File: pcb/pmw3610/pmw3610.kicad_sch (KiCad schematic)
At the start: 21 parts, among them J1 Conn_01x01_Socket, J2 Conn_01x01_Socket, J3 Conn_01x01_Socket, J5 Conn_01x01_Socket, J6 Conn_01x01_Socket, J7 Conn_01x01_Socket, J8 Conn_01x01_Socket, U1 TCR2EF19, U2 PMW3610

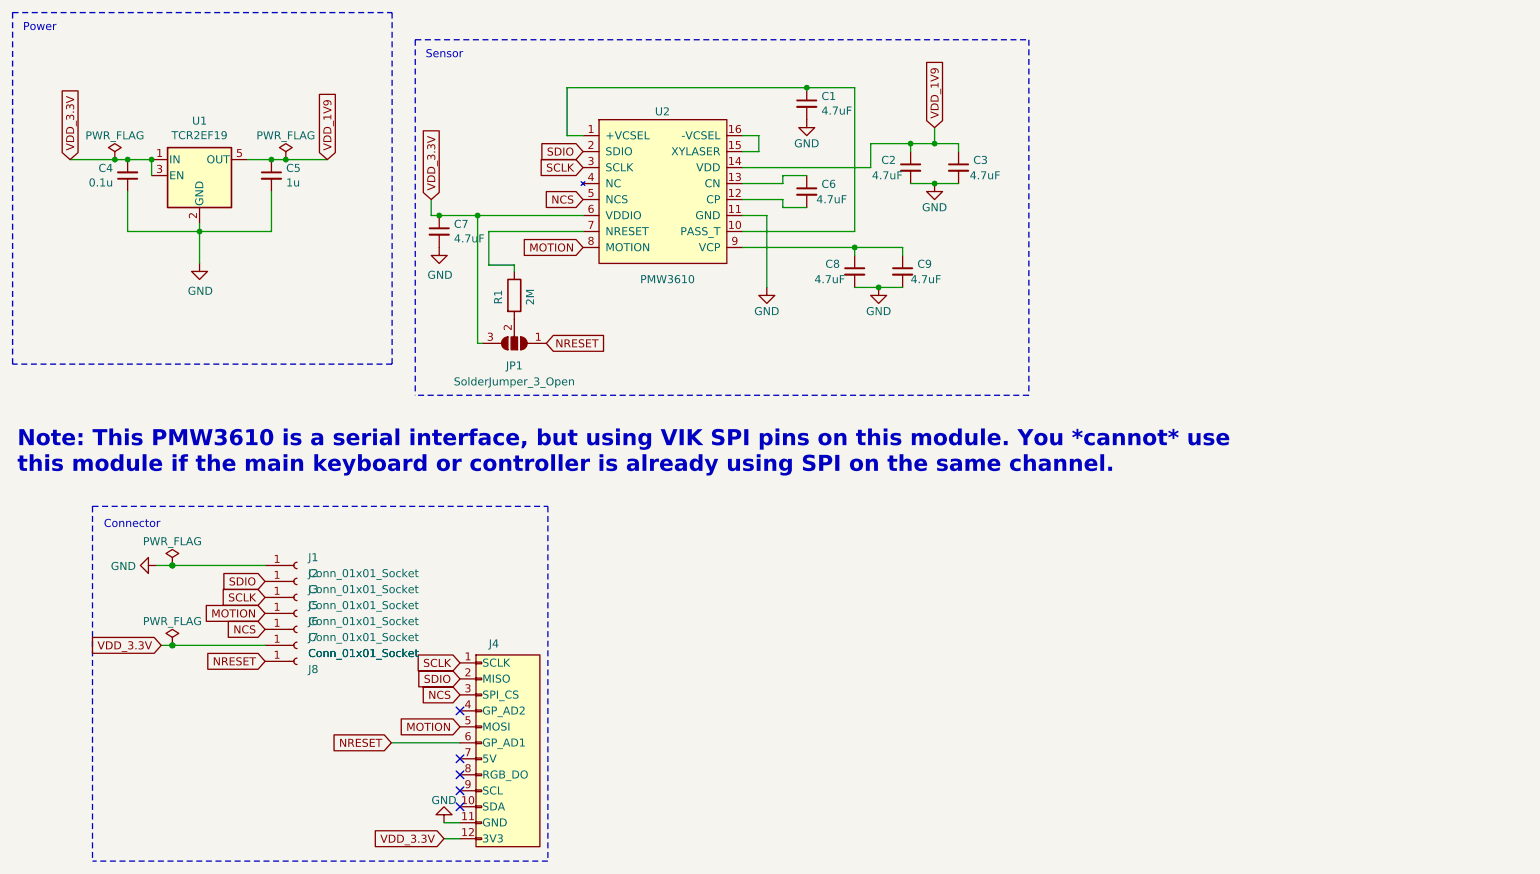
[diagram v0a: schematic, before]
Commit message: pcb: Update main and pmw3610 schematics
This should allow using PMW3610 and a nice!view display with the same SPI
pins on the controller:
- pmw3610: move MOTION (IRQ) signal to GPIO2 VIK wire
- pmw3610: move SDIO signal to MOSI VIK wire
- main: swap GPIO1/2 on the MCU so that GPIO2 is mapped to MISO
  Enables trackball without the extra 3-pin header

Update and reorgnanize configuration information.

Signed-off-by: Felix Kuehling <felix.kuehling@gmail.com>
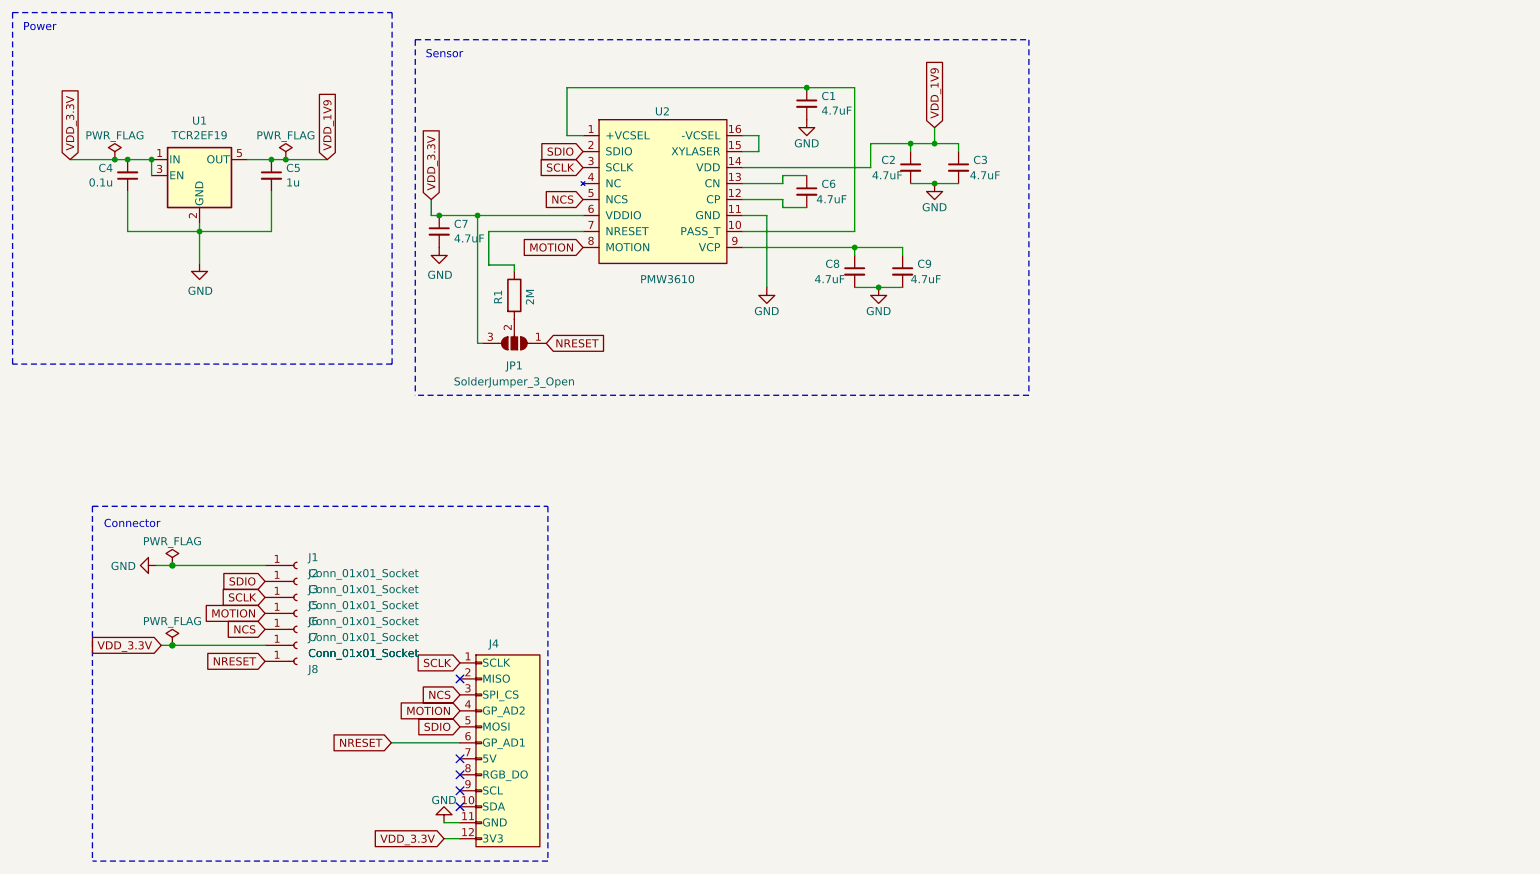
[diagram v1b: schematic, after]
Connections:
- net MOTION: now also J4.4 (GP_AD2); no longer J4.5 (MOSI)
- net SDIO: now also J4.5 (MOSI); no longer J4.2 (MISO)
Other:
- note removed: "Note: This PMW3610 is a serial interface, but using VIK SPI pins on this module. You *cannot* use this module if the main keyboard or controller is already using SPI on the same channel."
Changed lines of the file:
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@@
   (junction (at 75.438 51.816) (diameter 0) (color 0 0 0 0)
   )
-  (no_connect (at 105.41 139.446))
+  (no_connect (at 105.41 134.366))
   (no_connect (at 105.41 152.146))
   (no_connect (at 105.41 147.066))
@@
     (effects (font (size 1.27 1.27)) (justify right bottom))
   )
-  (text "Note: This PMW3610 is a serial interface, but using VIK SPI pins on this module. You *cannot* use\nthis module if the main keyboard or controller is already using SPI on the same channel."
-    (at 35.052 101.854 0)
-    (effects (font (size 2.54 2.54) (thickness 0.508) bold) (justify left bottom))
-  )
   (text "Sensor" (at 105.918 35.941 0)
     (effects (font (size 1.27 1.27)) (justify right bottom))
@@
     )
   )
-  (global_label "MOTION" (shape input) (at 105.41 141.986 180) (fields_autoplaced)
-    (effects (font (size 1.27 1.27)) (justify right))
-    (property "Intersheetrefs" "${INTERSHEET_REFS}" (at 95.3938 141.986 0)
+  (global_label "MOTION" (shape input) (at 105.41 139.446 180) (fields_autoplaced)
+    (effects (font (size 1.27 1.27)) (justify right))
+    (property "Intersheetrefs" "${INTERSHEET_REFS}" (at 95.3938 139.446 0)
       (effects (font (size 1.27 1.27)) (justify right) hide)
     )
@@
     )
   )
-  (global_label "SDIO" (shape input) (at 105.41 134.366 180) (fields_autoplaced)
-    (effects (font (size 1.27 1.27)) (justify right))
-    (property "Intersheetrefs" "${INTERSHEET_REFS}" (at 97.9943 134.366 0)
-      (effects (font (size 1.27 1.27)) (justify right) hide)
-    )
+  (global_label "SDIO" (shape input) (at 105.41 141.986 180) (fields_autoplaced)
+    (effects (font (size 1.27 1.27)) (justify right))
+    (property "Intersheetrefs" "${INTERSHEET_REFS}" (at 97.9943 141.986 0)
+      (effects (font (size 1.27 1.27)) (justify right) hide)
+    )
